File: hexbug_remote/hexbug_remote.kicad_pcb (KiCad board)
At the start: 2 copper layers, 65 x 36 mm, 38 parts, among them J1 USB_C_Receptacle_USB2.0_16P, J2 Conn_01x02, J3 Conn_01x06, SW1 SW_Push, SW2 SW_Push, SW3 SW_Push, SW4 SW_Push, SW5 SW_Push, SW6 SW_Push, SW7 SW_SP4T_6PIN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

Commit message: --Add Gerber Files
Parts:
- removed BT2: Battery_Cell, Button_Samesky:Battery_Holder_MPD_BCAAPC
- removed C7: 1uF, Capacitor_SMD:C_0603_1608Metric_Pad1.08x0.95mm_HandSolder
- added BT1: AA, Local_Footprints:Battery_Holder_MPD_BCAAPC, B.Cu at (106.9, 91.5)
- added C6: 1uF, Capacitor_SMD:C_0603_1608Metric, F.Cu at (106.9, 93.4)
- C1, C2, C3, C4, C5: footprint Capacitor_SMD:C_0603_1608Metric_Pad1.08x0.95mm_HandSolder -> Capacitor_SMD:C_0603_1608Metric
- D1: value Green -> Red
- D2: value Red -> Green
- D4: value LED -> IR
- J1: value USB_C_Receptacle_USB2.0_16P -> USB C; footprint Button_Samesky:USBC_16P -> Local_Footprints:USBC_16P
- R1, R2: value 5.1K -> 5.1k
- R3, R5, R6, R7, R8: value 1K -> 1k
- R4: value 10K -> 10k
- SW1, SW2, SW3, SW4, SW5, SW6: value SW_Push -> Tactile
- SW7: value SW_SP4T_6PIN -> SP4T; footprint Button_Samesky:SW_SPDT_Slide_Samesky_SLW-147844 -> Local_Footprints:SW_SP4T_Slide_Samesky_SLW-147844
- SW8: value SW_SPDT_3PIN -> SPDT; footprint Button_Samesky:SW_SPDT_Slide_Samesky_SLW-129956 -> Local_Footprints:SW_SPDT_Slide_CK_SK12D07VG4
- U1: value TLV70033_SOT23-5 -> BQ21040; footprint Package_TO_SOT_SMD:SOT-23-5 -> Package_TO_SOT_SMD:SOT-23-6
- U2: value MSPM01304xDGS20 -> RT9078; footprint Button_Samesky:TI_DGS20 -> Package_TO_SOT_SMD:SOT-23-5
- U3: value BQ21040DBV -> MSPM0L1304; footprint Package_TO_SOT_SMD:SOT-23-6 -> Local_Footprints:TI_DGS20
- moved D1 31.2 mm to (116.6, 99.2), turned to 0 degrees
- moved D3 31.0 mm to (90.3, 82.7), turned to -90 degrees
- moved R5 30.2 mm to (100.1, 76.7)
- moved R8 30.0 mm to (120.1, 99.1), turned to 180 degrees
- moved U3 24.8 mm to (92.4, 91.2)
- moved U1 15.7 mm to (114.6, 102.2), turned to 180 degrees
- moved U2 14.4 mm to (106.6, 88.6), turned to -90 degrees
- moved SW3 12.0 mm to (78.5, 94.8)
- moved SW4 12.0 mm to (78.5, 82.8)
- moved SW7 4.00 mm to (88.0, 105.9)
- moved SW8 3.07 mm to (125.0, 105.9)
- moved C1 0.66 mm to (108.5, 98.5)
- moved R1 0.16 mm to (98.9, 103.3)
- moved R2 0.16 mm to (97.4, 103.3)
- moved SW1 0.14 mm to (125.7, 75.1)
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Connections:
- C1 pad 1: Net-(U3-VIN) -> Net-(U1-VIN)
- C2 pad 1: Net-(BT2-+) -> Net-(BT1-+)
- C4 pad 1: Net-(U2-VCORE) -> Net-(U3-VCORE)
- D1 pad 1: GND -> Net-(D1-K)
- D3 pad 1: Net-(D3-K) -> GND
- J1 pad A4: Net-(U3-VIN) -> Net-(U1-VIN)
- J1 pad A9: Net-(U3-VIN) -> Net-(U1-VIN)
- J1 pad B4: Net-(U3-VIN) -> Net-(U1-VIN)
- J1 pad B9: Net-(U3-VIN) -> Net-(U1-VIN)
- J2 pad 1: Net-(BT2-+) -> Net-(BT1-+)
- JP1 pad 1: Net-(BT2-+) -> Net-(BT1-+)
- R3 pad 1: Net-(U3-ISET) -> Net-(U1-ISET)
- R4 pad 1: Net-(U3-TS) -> Net-(U1-TS)
- R5 pad 1: Net-(D3-A) -> +3V3
- R5 pad 2: Net-(BT2-+) -> Net-(D4-A)
- R6 pad 1: Net-(U2-PA16/A8) -> Net-(U3-PA16/A8)
- R7 pad 1: Net-(U2-PA11) -> Net-(U3-PA11)
- R7 pad 2: Net-(D1-A) -> Net-(D3-A)
- R8 pad 1: +3V3 -> Net-(BT1-+)
- R8 pad 2: Net-(D4-A) -> Net-(D1-A)
- SW1 pad 2: Net-(U2-PA4) -> Net-(U3-PA4)
- SW2 pad 2: Net-(U2-PA6) -> Net-(U3-PA6)
- SW3 pad 2: Net-(U2-PA17) -> Net-(U3-PA22/A4)
- SW4 pad 2: Net-(U2-PA22/A4) -> Net-(U3-PA17)
- SW5 pad 2: Net-(U2-PA27/A0) -> Net-(U3-PA27/A0)
- SW6 pad 2: Net-(U2-PA26/A1) -> Net-(U3-PA26/A1)
- SW7 pad 1: Net-(U2-PA18/A7) -> Net-(U3-PA18/A7)
- SW7 pad 2: Net-(U2-PC25/A2) -> Net-(U3-PC25/A2)
- SW7 pad 5: Net-(U2-PA24/A3) -> Net-(U3-PA24/A3)
- SW7 pad 6: Net-(U2-PA23) -> Net-(U3-PA23)
- SW8 pad 2: Net-(U1-EN) -> Net-(U2-EN)
- U1 pad 1: Net-(J2-Pin_2) -> Net-(U1-TS)
- U1 pad 2: GND -> Net-(BT1-+)
- U1 pad 3: Net-(U1-EN) -> Net-(D1-K)
- U1 pad 4: unconnected-(U1-NC-Pad4) -> Net-(U1-ISET)
- U1 pad 5: +3V3 -> GND
- U2 pad 1: Net-(U2-PA26/A1) -> Net-(J2-Pin_2)
- U2 pad 2: Net-(U2-PA27/A0) -> GND
- U2 pad 3: Net-(U2-VCORE) -> Net-(U2-EN)
- U2 pad 4: Net-(D4-K) -> unconnected-(U2-NC-Pad4)
- U2 pad 5: Net-(J3-Pin_1) -> +3V3
- U3 pad 1: Net-(U3-TS) -> Net-(U3-PA26/A1)
- U3 pad 2: Net-(BT2-+) -> Net-(U3-PA27/A0)
- U3 pad 3: Net-(D3-K) -> Net-(U3-VCORE)
- U3 pad 4: Net-(U3-ISET) -> Net-(D4-K)
- U3 pad 5: GND -> Net-(J3-Pin_1)
- U3 pad 6: Net-(U3-VIN) -> +3V3
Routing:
- net Net-(BT2-+): track 60.3 -> 0.00 mm
- net Net-(BT1-+): track 0.00 -> 60.3 mm
- net Net-(U3-PA26/A1): track 0.00 -> 43.8 mm
- net Net-(U2-PA26/A1): track 43.8 -> 0.00 mm
- net Net-(U3-PA4): track 0.00 -> 40.5 mm
- net Net-(U2-PA4): track 40.5 -> 0.00 mm
- net Net-(U2-EN): track 0.00 -> 37.1 mm, vias 0 -> 4
- net Net-(U1-EN): track 37.1 -> 0.00 mm, vias 4 -> 0
- net Net-(U3-PA27/A0): track 0.00 -> 31.6 mm
- net Net-(U2-PA27/A0): track 31.6 -> 0.00 mm
- net Net-(U3-PA6): track 0.00 -> 22.2 mm
- net Net-(U2-PA6): track 22.2 -> 0.00 mm
- net Net-(U1-VIN): track 0.00 -> 21.8 mm, vias 0 -> 2
- net Net-(U3-VIN): track 21.2 -> 0.00 mm, vias 2 -> 0
- net Net-(U2-PA23): track 17.8 -> 0.00 mm
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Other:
- board text added: "Hexbug Remote Rev 1"

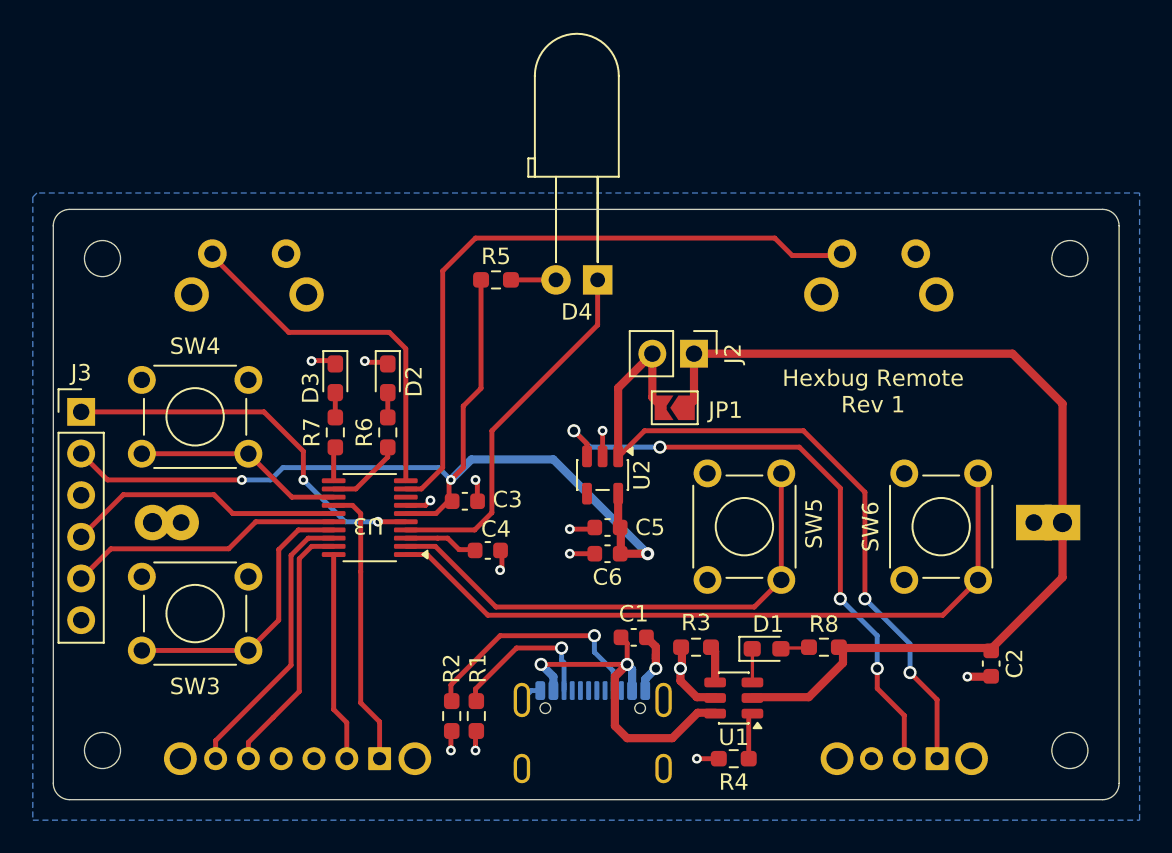
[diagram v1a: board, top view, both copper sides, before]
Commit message: Add Battery Protection
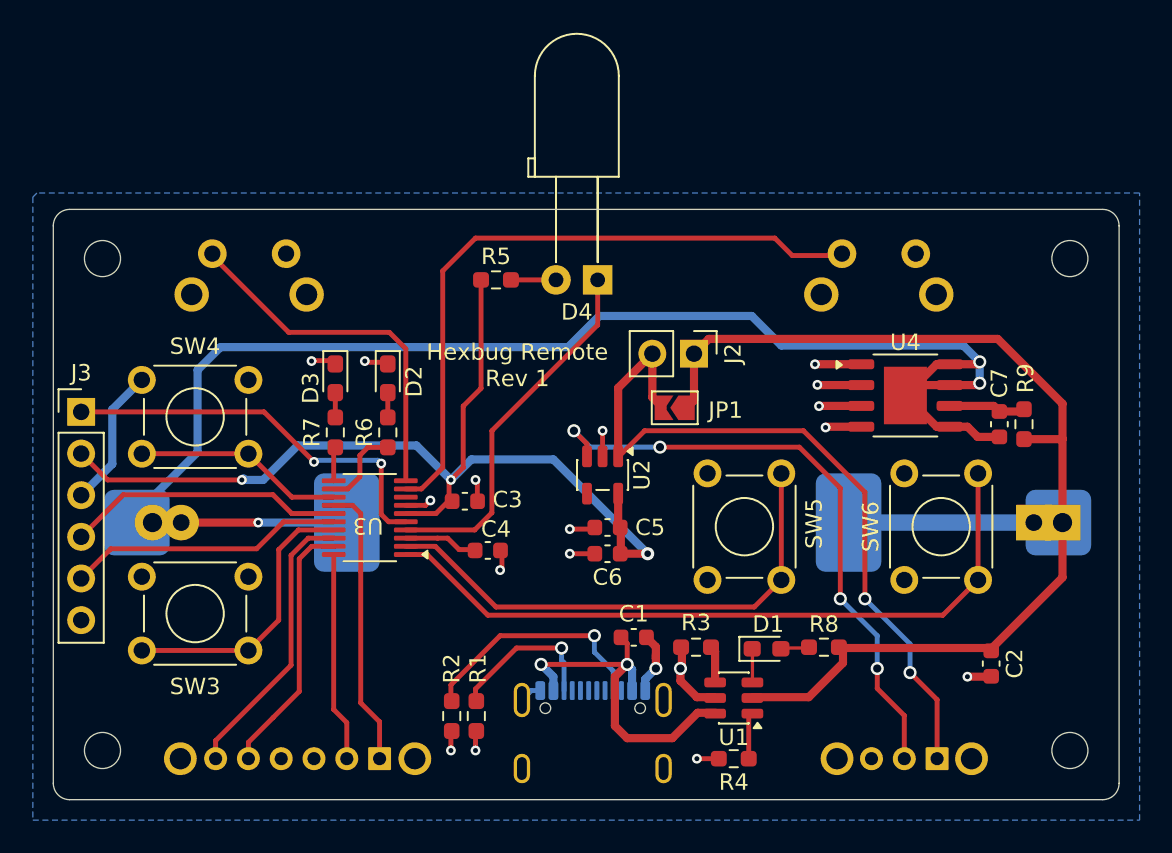
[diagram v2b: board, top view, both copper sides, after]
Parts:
- added C7: 0.1uF, Capacitor_SMD:C_0603_1608Metric, F.Cu at (130.8, 85.5)
- added J4, J5: AA, Local_Footprints:Battery_Clip_Keystone_53, B.Cu at (106.3, 91.5)
- added R9: 1k, Resistor_SMD:R_0603_1608Metric_Pad0.98x0.95mm_HandSolder, F.Cu at (132.3, 85.5)
- added U4: XB8089D0, Local_Footprints:SOP-8-1EP_3.9x4.9mm_P1.27mm_EP2.4x3.3mm, F.Cu at (125.1, 83.8)
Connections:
- BT1 pad 2: GND -> Net-(BT1--)
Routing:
- net Net-(BT1--): track 0.00 -> 91.7 mm, vias 0 -> 3
- net GND: track 27.0 -> 45.9 mm, vias 14 -> 18
- net Net-(BT1-+): track 60.3 -> 76.4 mm
- net Net-(U4-VDD): track 0.00 -> 4.73 mm
- net +3V3: track 61.3 -> 62.3 mm
- net Net-(J3-Pin_1): track 23.7 -> 24.5 mm

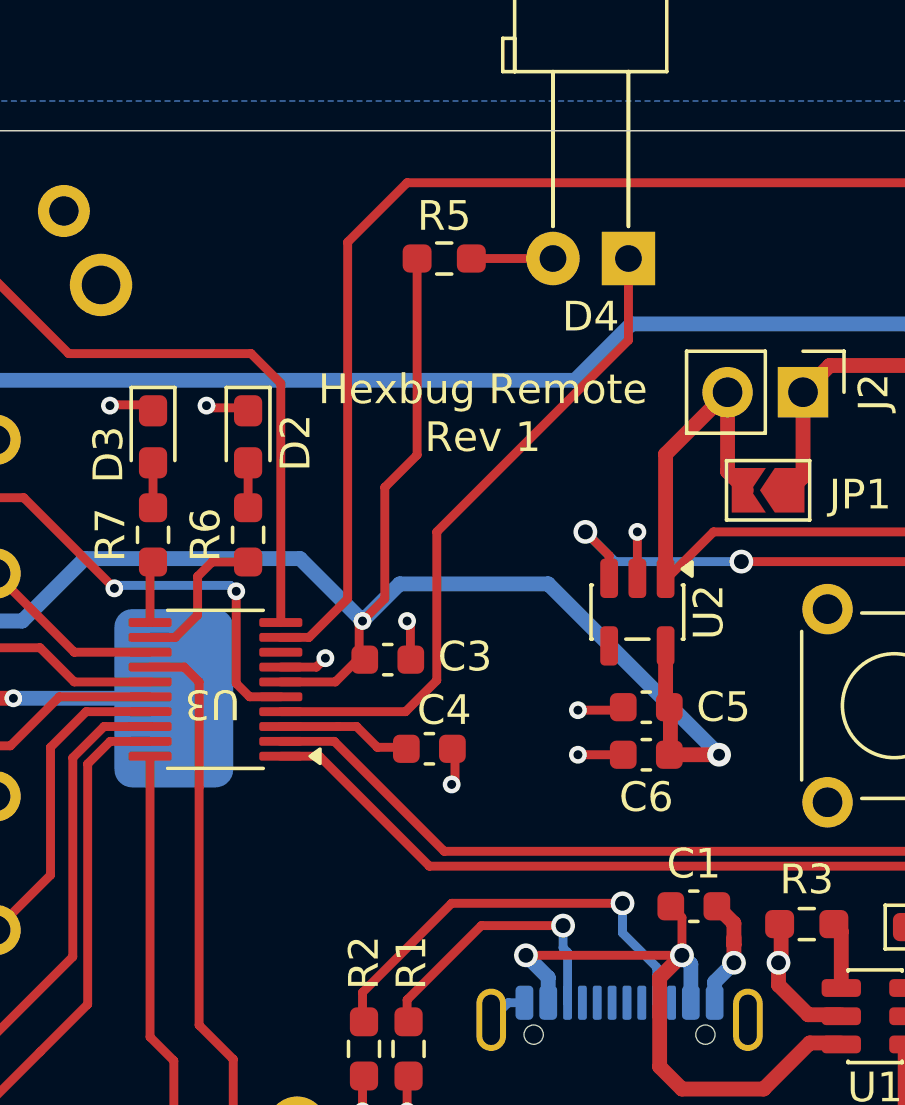
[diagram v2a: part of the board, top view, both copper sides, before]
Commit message: Add Firmware Update PCB to Rev 2 --Pull up resistor for reset
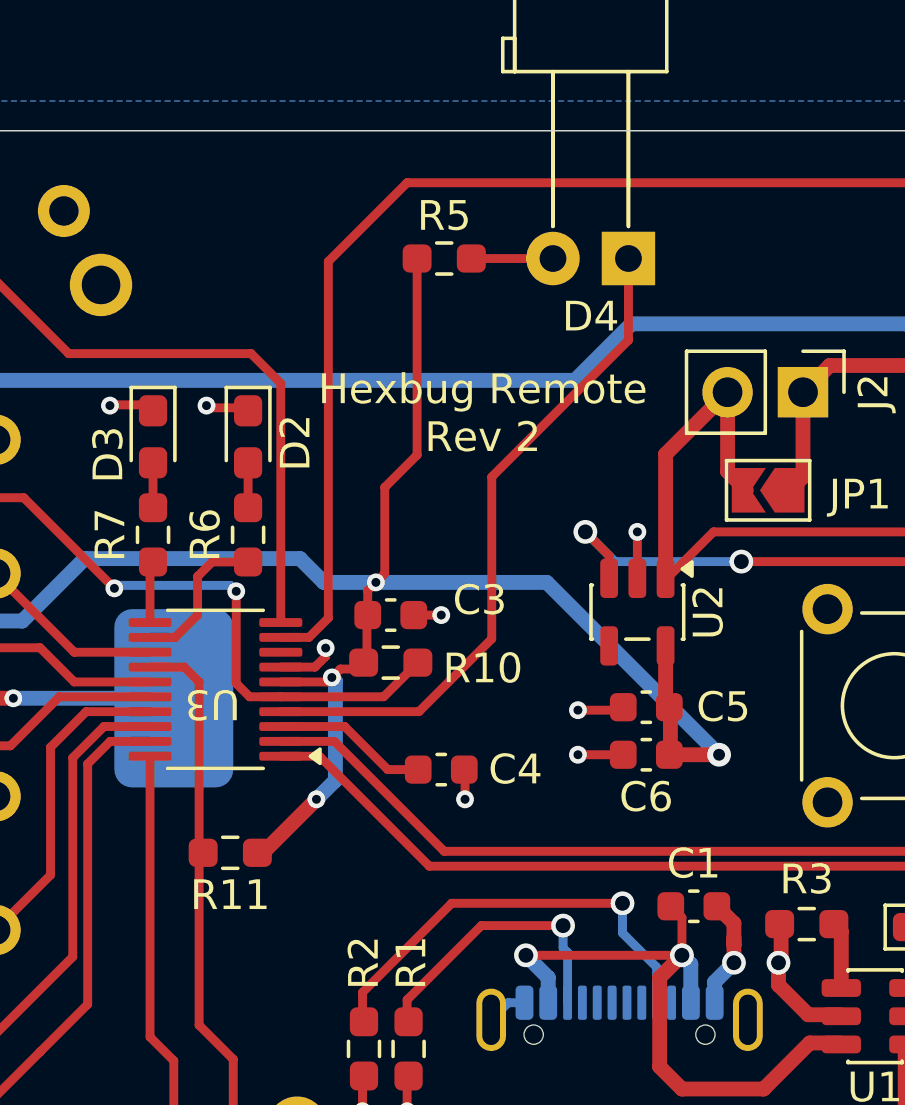
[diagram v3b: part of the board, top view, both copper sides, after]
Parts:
- added R10: 10k, Resistor_SMD:R_0603_1608Metric_Pad0.98x0.95mm_HandSolder, F.Cu at (98.3, 90.3)
- added R11: 10k, Resistor_SMD:R_0603_1608Metric_Pad0.98x0.95mm_HandSolder, F.Cu at (92.9, 96.7)
- moved C3 1.50 mm to (98.3, 88.7)
- moved C4 0.81 mm to (100.0, 93.9)
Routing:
- net +3V3: track 62.3 -> 68.6 mm, vias 3 -> 5
- net Net-(J3-Pin_1): track 24.5 -> 29.6 mm
- net Net-(U3-VCORE): track 4.43 -> 5.23 mm
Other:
- board text added: "Hexbug Remote Rev 2"
- board text removed: "Hexbug Remote Rev 1"
